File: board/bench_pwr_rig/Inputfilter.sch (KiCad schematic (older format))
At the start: 9 parts

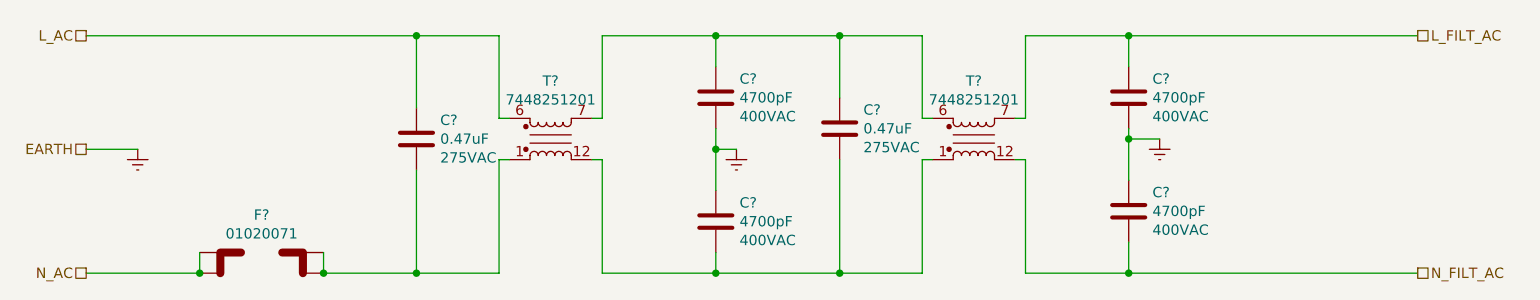
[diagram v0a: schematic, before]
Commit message: schematic and layout updates
Finalized schematic for rev 0.1. Anticipate additional component values update through analysis. Moving to layout
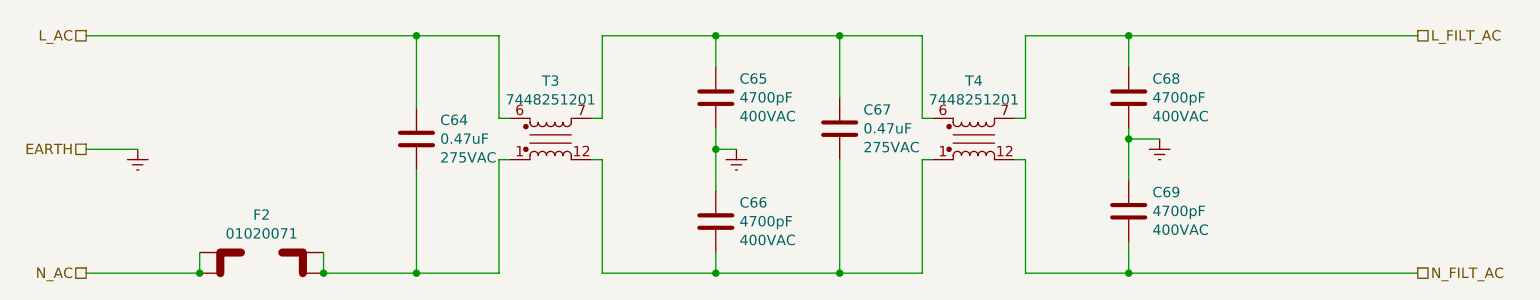
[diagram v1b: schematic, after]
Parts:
- gave numbers to parts that had none: 9
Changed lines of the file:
@@
 $EndDescr
 $Comp
-L Filter:7448251201 T?
+L Filter:7448251201 T4
 U 1 1 5FBA8028
 P 6500 3250
-F 0 "T?" H 6500 3531 50  0000 C CNN
+F 0 "T4" H 6500 3531 50  0000 C CNN
 F 1 "7448251201" H 6500 3440 50  0000 C CNN
 F 2 "Transformer_THT:Choke_Wurth_7448251201" H 6500 3250 50  0001 C CNN
@@
 $EndComp
 $Comp
-L Filter:7448251201 T?
+L Filter:7448251201 T3
 U 1 1 5FBA802E
 P 4450 3250
-F 0 "T?" H 4450 3531 50  0000 C CNN
+F 0 "T3" H 4450 3531 50  0000 C CNN
 F 1 "7448251201" H 4450 3440 50  0000 C CNN
 F 2 "Transformer_THT:Choke_Wurth_7448251201" H 4450 3250 50  0001 C CNN
@@
 	7250 3200 7250 3250
 $Comp
-L power:Earth #PWR?
+L power:Earth #PWR071
 U 1 1 5FBA803A
 P 5350 3300
-F 0 "#PWR?" H 5350 3050 50  0001 C CNN
+F 0 "#PWR071" H 5350 3050 50  0001 C CNN
 F 1 "Earth" H 5350 3150 50  0001 C CNN
 F 2 "" H 5350 3300 50  0001 C CNN
@@
 $EndComp
 $Comp
-L power:Earth #PWR?
+L power:Earth #PWR072
 U 1 1 5FBA8040
 P 7400 3250
-F 0 "#PWR?" H 7400 3000 50  0001 C CNN
+F 0 "#PWR072" H 7400 3000 50  0001 C CNN
 F 1 "Earth" H 7400 3100 50  0001 C CNN
 F 2 "" H 7400 3250 50  0001 C CNN
@@
 	4200 3350 4200 3900
 $Comp
-L power:Earth #PWR?
+L power:Earth #PWR070
 U 1 1 5FBA8087
 P 2450 3300
-F 0 "#PWR?" H 2450 3050 50  0001 C CNN
+F 0 "#PWR070" H 2450 3050 50  0001 C CNN
 F 1 "Earth" H 2450 3150 50  0001 C CNN
 F 2 "" H 2450 3300 50  0001 C CNN
@@
 N_AC
 $Comp
-L Capacitor:ECQ-U2A474ML C?
+L Capacitor:ECQ-U2A474ML C64
 U 1 1 605933CC
 P 3800 3250
-F 0 "C?" H 3915 3341 50  0000 L CNN
+F 0 "C64" H 3915 3341 50  0000 L CNN
 F 1 "ECQ-U2A474ML" H 4200 3100 50  0001 C CNN
 F 2 "Capacitor_THT:C_Rect_L26.5mm_W8.5mm_P22.50mm_MKS4" H 3800 3250 50  0001 C CNN
@@
 	2200 2750 3800 2750
 $Comp
-L Capacitor:ECQ-U2A474ML C?
+L Capacitor:ECQ-U2A474ML C67
 U 1 1 6059A6C1
 P 5850 3200
-F 0 "C?" H 5965 3291 50  0000 L CNN
+F 0 "C67" H 5965 3291 50  0000 L CNN
 F 1 "ECQ-U2A474ML" H 6250 3050 50  0001 C CNN
 F 2 "Capacitor_THT:C_Rect_L26.5mm_W8.5mm_P22.50mm_MKS4" H 5850 3200 50  0001 C CNN
@@
 	5850 3900 6250 3900
 $Comp
-L Capacitor:C961U472MYWDBA7317 C?
+L Capacitor:C961U472MYWDBA7317 C65
 U 1 1 605A4581
 P 5250 3050
-F 0 "C?" H 5365 3141 50  0000 L CNN
+F 0 "C65" H 5365 3141 50  0000 L CNN
 F 1 "C961U472MYWDBA7317" H 5800 2850 50  0001 C CNN
 F 2 "Capacitor_THT:C_Disc_D14.5mm_W5.0mm_P10.00mm" H 5250 3050 50  0001 C CNN
@@
 $EndComp
 $Comp
-L Capacitor:C961U472MYWDBA7317 C?
+L Capacitor:C961U472MYWDBA7317 C66
 U 1 1 605A50DA
 P 5250 3650
-F 0 "C?" H 5365 3741 50  0000 L CNN
+F 0 "C66" H 5365 3741 50  0000 L CNN
 F 1 "C961U472MYWDBA7317" H 5800 3450 50  0001 C CNN
 F 2 "Capacitor_THT:C_Disc_D14.5mm_W5.0mm_P10.00mm" H 5250 3650 50  0001 C CNN
@@
 $EndComp
 $Comp
-L Capacitor:C961U472MYWDBA7317 C?
+L Capacitor:C961U472MYWDBA7317 C68
 U 1 1 605A54D1
 P 7250 3050
-F 0 "C?" H 7365 3141 50  0000 L CNN
+F 0 "C68" H 7365 3141 50  0000 L CNN
 F 1 "C961U472MYWDBA7317" H 7800 2850 50  0001 C CNN
 F 2 "Capacitor_THT:C_Disc_D14.5mm_W5.0mm_P10.00mm" H 7250 3050 50  0001 C CNN
@@
 $EndComp
 $Comp
-L Capacitor:C961U472MYWDBA7317 C?
+L Capacitor:C961U472MYWDBA7317 C69
 U 1 1 605A5A14
 P 7250 3600
-F 0 "C?" H 7365 3691 50  0000 L CNN
+F 0 "C69" H 7365 3691 50  0000 L CNN
 F 1 "C961U472MYWDBA7317" H 7800 3400 50  0001 C CNN
 F 2 "Capacitor_THT:C_Disc_D14.5mm_W5.0mm_P10.00mm" H 7250 3600 50  0001 C CNN
@@
 	7250 3900 8650 3900
 $Comp
-L Device:01020071 F?
+L Device:01020071 F2
 U 1 1 6060E5DB
 P 3050 3800
-F 0 "F?" H 3050 3982 50  0000 C CNN
+F 0 "F2" H 3050 3982 50  0000 C CNN
 F 1 "01020071" H 3050 3891 50  0000 C CNN
 F 2 "Fuse:Fuseholder_Littelfuse_0.25inD_1.25inL" H 3050 3800 50  0001 C CNN

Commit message: Updated layout
Added output screw terminal
Added mounting screws M4
Changed primary ground to secondary ground plane coupling capacitor to radial disc type with safety rating X1, Y1
Continued layout
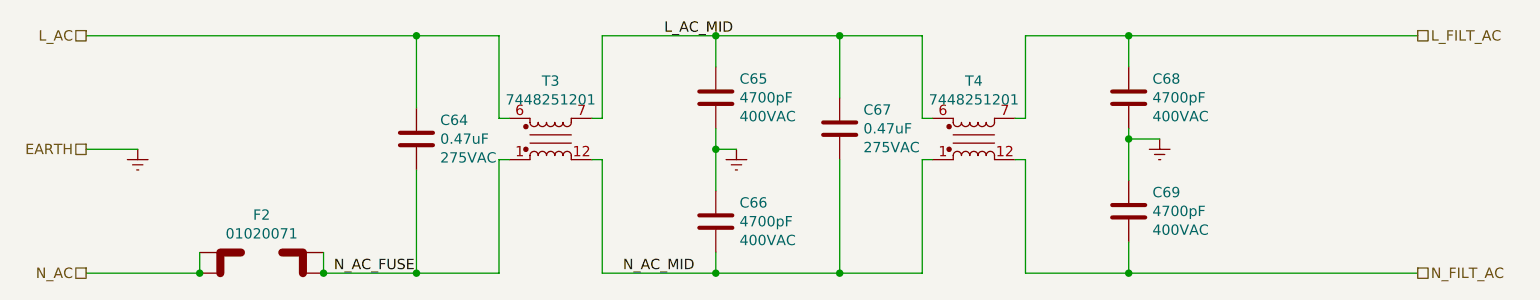
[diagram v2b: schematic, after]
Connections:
- net N_AC_MID: now reaches C66.2, C67.2, T3.12, T4.1
- net L_AC_MID: now reaches C65.1, C67.1, T3.7, T4.6
- net N_AC_FUSE: now reaches C64.2, F2.3, F2.4, T3.1
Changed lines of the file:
@@
 Connection ~ 3350 3900
 Connection ~ 3800 3900
+Text Label 3400 3900 0    50   ~ 0
+N_AC_FUSE
+Text Label 5000 2750 0    50   ~ 0
+L_AC_MID
+Text Label 4800 3900 0    50   ~ 0
+N_AC_MID
 $EndSCHEMATC
